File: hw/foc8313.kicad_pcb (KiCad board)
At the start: 2 copper layers, 70 parts, among them CN1 XT30PW-M, CN2 XT30PW-M, J1 Tag Connect, J2 CAN, J3 CAN, P1 USB_C_Plug, U1 DRV8313PWP, U10 XC6206P332MR, U2 STM32F103CBTx, U3 AS5047D, U4 INA240A2D, U5 INA240A2D, U7 LMR36015SFBRNXR, U8 INA240A2D, U9 ADM3053BRW_C579192, X1 X322516MLB4SI

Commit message: WIP XT30?
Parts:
- added FB1: 1.8k@100MHz, Resistor_SMD:R_0402_1005Metric, F.Cu at (190.2, 110.7)
- added FB2: 1.8k@100MHz, Resistor_SMD:R_0402_1005Metric, F.Cu at (190.2, 112.7)
- added U6: MR30PW-M30.G.Y, easyeda:CONN-TH_MR30PW-M30-G-Y, F.Cu at (140.6, 112.0)
- C20, C4, C7, P1, R12, R15, R4, R8, U3: moved to B.Cu
- J2, J3: footprint Connector_JST:JST_GH_SM04B-GHS-TB_1x04-1MP_P1.25mm_Horizontal -> Connector_JST:JST_GH_SM03B-GHS-TB_1x03-1MP_P1.25mm_Horizontal; moved to B.Cu
- moved U9 86.9 mm to (127.3, 101.7), turned to -90 degrees
- moved CN1 86.3 mm to (127.0, 86.5), turned to 180 degrees
- moved CN2 74.7 mm to (153.2, 86.5), turned to 180 degrees
- moved D2 68.5 mm to (118.0, 19.0)
- moved C10 68.5 mm to (98.5, 16.3)
- moved C12 68.5 mm to (98.5, 21.4)
- moved C13 68.5 mm to (98.5, 23.9)
- moved C14 68.5 mm to (117.3, 21.2)
- moved C15 68.5 mm to (117.3, 23.2)
- moved C22 68.5 mm to (115.5, 30.9)
- moved C23 68.5 mm to (94.5, 51.3)
- moved C26 68.5 mm to (115.4, 51.3)
- moved C3 68.5 mm to (94.5, 21.4)
- moved C5 68.5 mm to (94.5, 23.9)
- moved C8 68.5 mm to (94.5, 31.4)
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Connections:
- C1 pad 2: +3.3V -> GND
- C10 pad 2: +3.3V -> GND
- C11 pad 2: +3.3V -> GND
- C12 pad 2: +3.3V -> GND
- C13 pad 2: +3.3V -> GND
- C14 pad 2: +3.3V -> GND
- C15 pad 1: +3.3V -> GND
- C16 pad 2: +3.3V -> GND
- C17 pad 2: +3.3V -> GND
- C19 pad 2: +3.3V -> GND
- C2 pad 2: +3.3V -> GND
- C20 pad 2: +3.3V -> GND
- C22 pad 2: +3.3V -> GND
- C23 pad 2: +3.3V -> GND
- C24 pad 2: +3.3V -> GND
- C26 pad 2: +3.3V -> GND
- C27 pad 2: +3.3V -> GND
- C30 pad 2: +3.3V -> GND
- C31 pad 2: +3.3V -> GND
- C32 pad 2: +3.3V -> GND
- C33 pad 2: +3.3V -> GND
- C4 pad 2: +3.3V -> GND
- C5 pad 2: +3.3V -> GND
- C6 pad 2: +3.3V -> GND
- C7 pad 2: +3.3V -> GND
- C9 pad 2: +3.3V -> GND
- CN1 pad 1: +3.3V -> VCC
- CN1 pad 2: VCC -> GND
- CN2 pad 1: +3.3V -> VCC
- CN2 pad 2: VCC -> GND
- J1 pad 5: +3.3V -> GND
- P1 pad A1: +3.3V -> GND
- P1 pad A12: +3.3V -> GND
- P1 pad B1: +3.3V -> GND
- P1 pad B12: +3.3V -> GND
- R11 pad 2: +3.3V -> GND
- R13 pad 2: +3.3V -> GND
- R3 pad 1: +3.3V -> GND
- R5 pad 2: +3.3V -> GND
- U1 pad 10: +3.3V -> GND
- U1 pad 14: +3.3V -> GND
- U1 pad 20: +3.3V -> GND
- U1 pad 28: +3.3V -> GND
- U1 pad 29: +3.3V -> GND
- U1 pad 6: +3.3V -> GND
- U1 pad 7: +3.3V -> GND
- U10 pad 1: +3.3V -> GND
- U2 pad 23: +3.3V -> GND
- U2 pad 35: +3.3V -> GND
- U2 pad 47: +3.3V -> GND
- U3 pad 13: +3.3V -> GND
- U3 pad 5: +3.3V -> GND
- U4 pad 2: +3.3V -> GND
- U4 pad 3: +3.3V -> GND
- U4 pad 4: +3.3V -> GND
- U5 pad 2: +3.3V -> GND
- U5 pad 3: +3.3V -> GND
- U5 pad 4: +3.3V -> GND
- U7 pad 1: +3.3V -> GND
- U7 pad 11: +3.3V -> GND
- U7 pad 6: +3.3V -> GND
- U8 pad 2: +3.3V -> GND
- U8 pad 3: +3.3V -> GND
- U8 pad 4: +3.3V -> GND
- U9 pad 1: +3.3V -> GND
- U9 pad 10: +3.3V -> GND
- U9 pad 3: +3.3V -> GND
- U9 pad 7: +3.3V -> GND
- U9 pad 9: +3.3V -> GND
- X1 pad 2: +3.3V -> GND
- X1 pad 4: +3.3V -> GND
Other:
- board outline added: 40 x 40 mm

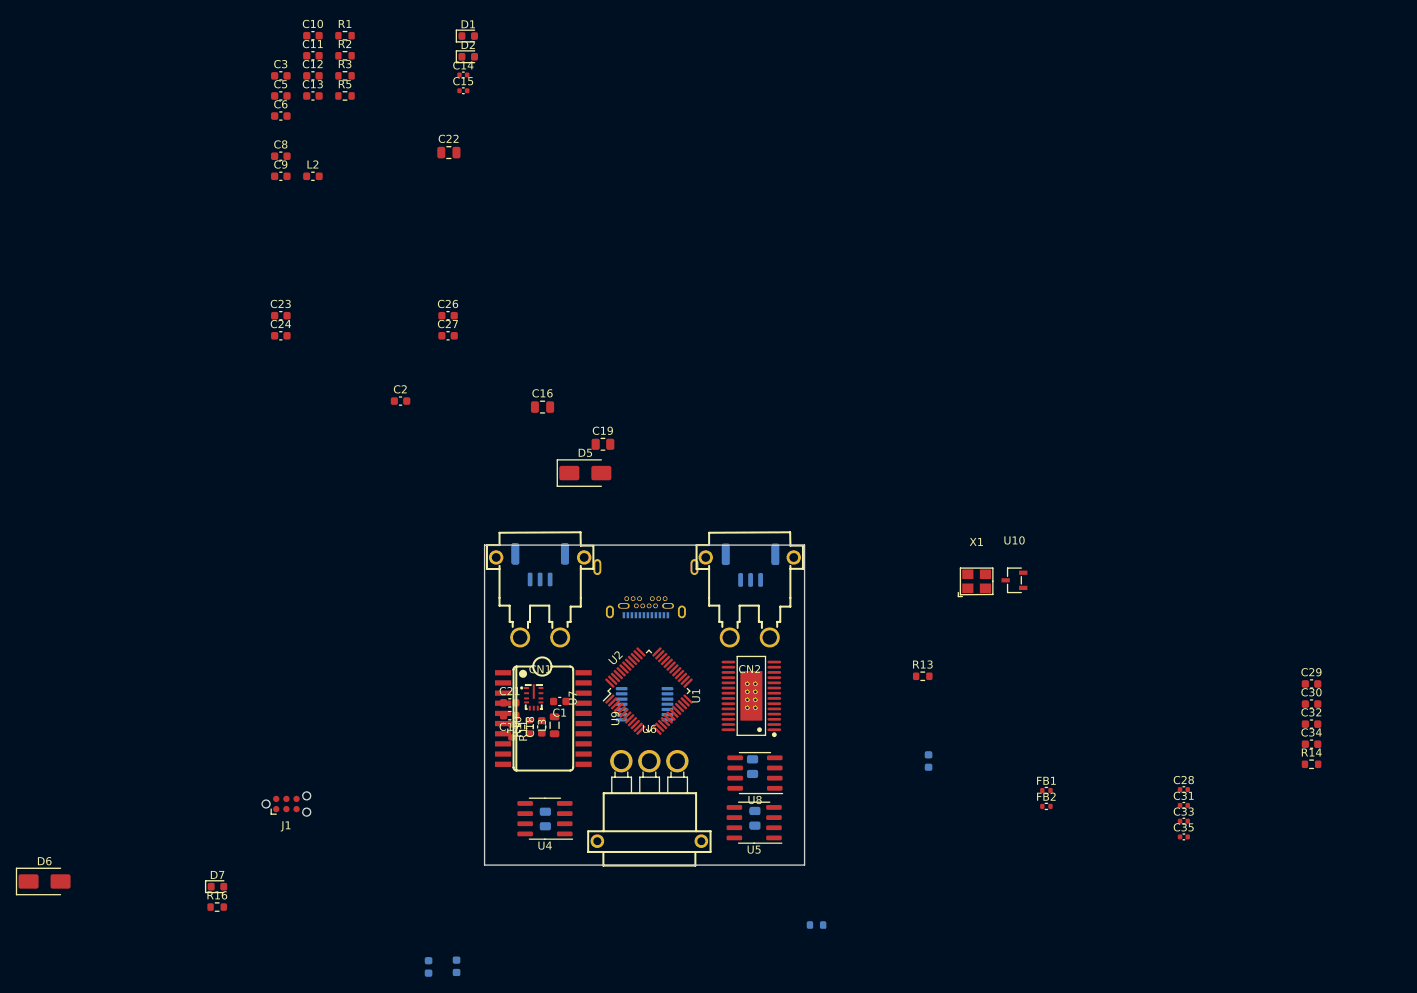
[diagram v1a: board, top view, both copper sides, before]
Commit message: [Hw] No iso can, 0402 where possible, approx layout and formfactor
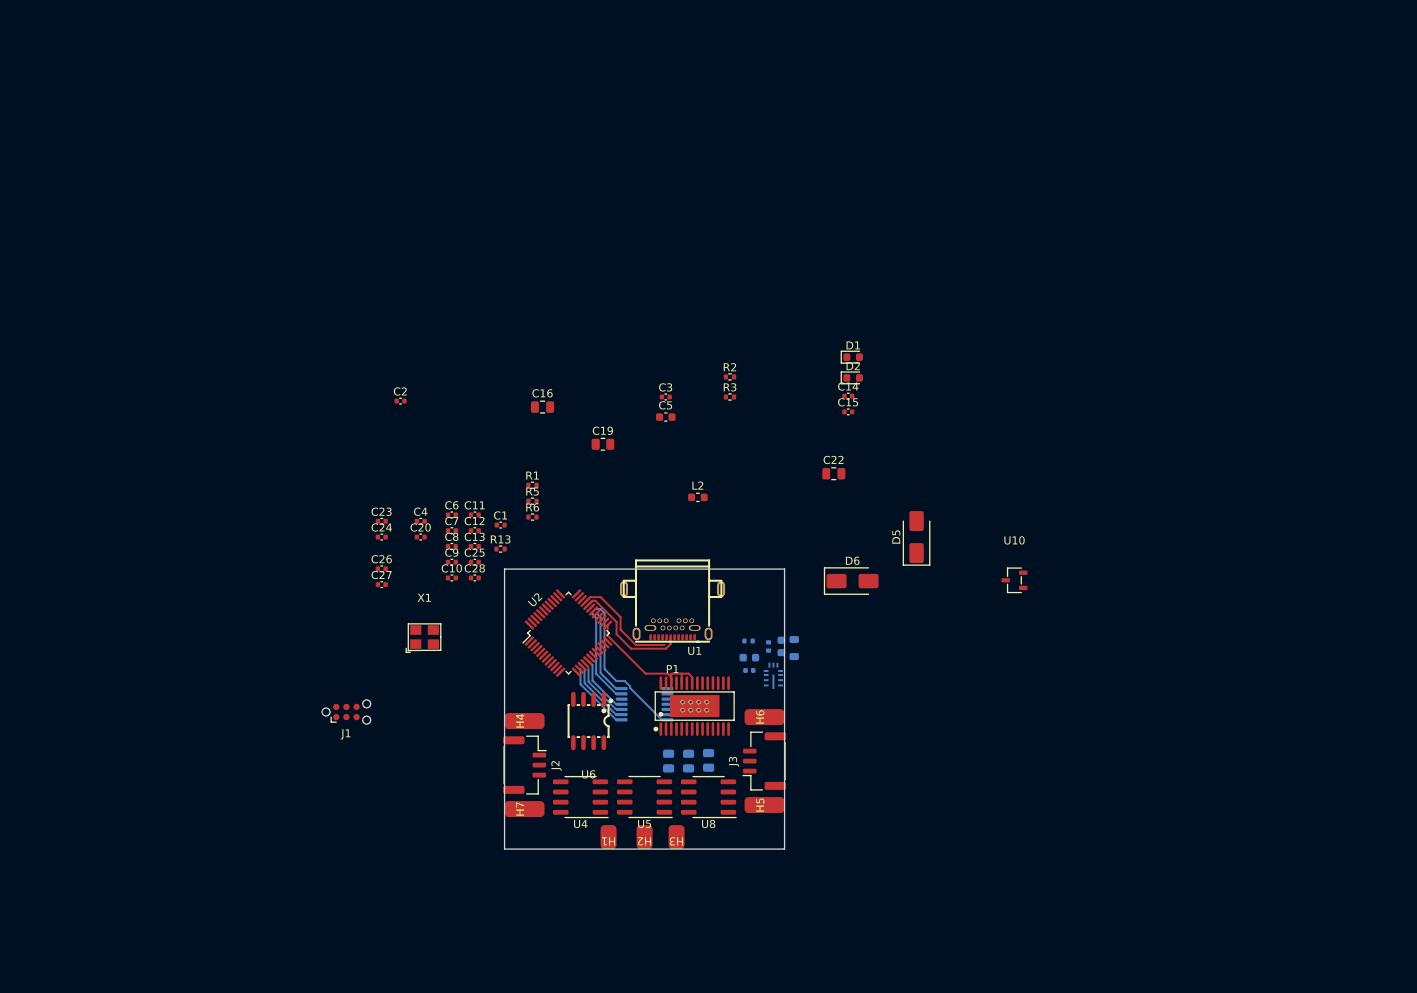
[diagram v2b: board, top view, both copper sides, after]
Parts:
- removed C29, C30, C32, C34: 10u, Capacitor_SMD:C_0603_1608Metric
- removed C31, C33, C35: 100n, Capacitor_SMD:C_0402_1005Metric
- removed CN1, CN2: XT30PW-M, easyeda:CONN-TH_XT30PW-M
- removed D7: BLUE, LED_SMD:LED_0603_1608Metric
- removed FB1, FB2: 1.8k@100MHz, Resistor_SMD:R_0402_1005Metric
- removed R12: 100k, Resistor_SMD:R_0603_1608Metric
- removed R14: 120, Resistor_SMD:R_0603_1608Metric
- removed R16: 1k5, Resistor_SMD:R_0603_1608Metric
- removed U9: ADM3053BRW_C579192, easyeda:SO-20_L12.8-W7.5-P1.27-LS10.3-BL
- added C25: 100n, Capacitor_SMD:C_0402_1005Metric, F.Cu at (118.8, 82.1)
- added H1: MountingHole_Pad, local_lib:2x3, F.Cu at (135.5, 116.5)
- added H2: MountingHole_Pad, local_lib:2x3, F.Cu at (140.0, 116.5)
- added H3: MountingHole_Pad, local_lib:2x3, F.Cu at (144.0, 116.5)
- added H4: MountingHole_Pad, local_lib:2x5, F.Cu at (125.0, 102.0)
- added H5: MountingHole_Pad, local_lib:2x5, F.Cu at (155.0, 112.5)
- added H6: MountingHole_Pad, local_lib:2x5, F.Cu at (155.0, 101.5)
- added H7: MountingHole_Pad, local_lib:2x5, F.Cu at (125.0, 113.0)
- added R6: 100k, Resistor_SMD:R_0402_1005Metric, F.Cu at (126.0, 76.5)
- C1, C10, C11, C12, C13, C2, C23, C24, C26, C27, C3, C6, C8, C9: footprint Capacitor_SMD:C_0603_1608Metric -> Capacitor_SMD:C_0402_1005Metric
- C17, C18, L3, U7: moved to B.Cu
- C20, C4, C7: footprint Capacitor_SMD:C_0603_1608Metric -> Capacitor_SMD:C_0402_1005Metric; moved to F.Cu
- C21: footprint Capacitor_SMD:C_0603_1608Metric -> Capacitor_SMD:C_0402_1005Metric; moved to B.Cu
- J2, J3, P1: moved to F.Cu
- R1, R13, R2, R3, R5: footprint Resistor_SMD:R_0603_1608Metric -> Resistor_SMD:R_0402_1005Metric
- R10, R11: footprint Resistor_SMD:R_0603_1608Metric -> Resistor_SMD:R_0402_1005Metric; moved to B.Cu
- U6: value MR30PW-M30.G.Y -> TJA1044GT/3Z; footprint easyeda:CONN-TH_MR30PW-M30-G-Y -> easyeda:SO-8_L4.9-W3.9-P1.27-LS5.9-BL
- moved D6 107.8 mm to (166.0, 84.5)
- moved C28 92.5 mm to (118.8, 84.1)
- moved C10 70.0 mm to (115.9, 84.1)
- moved X1 69.4 mm to (112.5, 91.5)
- moved C7 66.2 mm to (115.9, 78.2), turned to 0 degrees
- moved C14 62.7 mm to (165.5, 61.4)
- moved C15 62.7 mm to (165.5, 63.4)
- moved C22 62.7 mm to (163.7, 71.1)
- moved C3 62.7 mm to (142.7, 61.5)
- moved C5 62.7 mm to (142.7, 64.0)
- moved R2 62.7 mm to (150.7, 59.0)
- moved R3 62.7 mm to (150.7, 61.5)
- moved D1 62.7 mm to (166.1, 56.5)
- moved D2 62.7 mm to (166.1, 59.1)
- moved L2 62.7 mm to (146.7, 74.0)
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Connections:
- C28 pad 1: /isocan/ISOGND -> +3.3V
- C28 pad 2: /isocan/CAN.V+ -> GND
- U6 pad 1: /OUTA -> /CAN.TX
- U6 pad 2: /OUTB -> GND
- U6 pad 3: /OUTC -> +5V
- U6 pad 4: unconnected-(U6-Pad4) -> /CAN.RX
- U6 pad 5: unconnected-(U6-Pad5) -> +3.3V
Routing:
- net /ENC_Z: track 0.00 -> 18.8 mm
- net /DRV_EN: track 0.00 -> 18.0 mm
- net /USB_DM: track 0.00 -> 15.0 mm
- net /USB_DP: track 0.00 -> 13.6 mm
- net /ENC_B: track 0.00 -> 12.0 mm
- net /ENC_A: track 0.00 -> 11.2 mm
- net /~{SPI1_NSS}: track 0.00 -> 8.88 mm
- net /SPI1_SCLK: track 0.00 -> 8.02 mm
- net /SPI1_MOSI: track 0.00 -> 7.52 mm
- net /SPI1_MISO: track 0.00 -> 7.17 mm
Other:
- board size 40 x 40 mm -> 35 x 35 mm

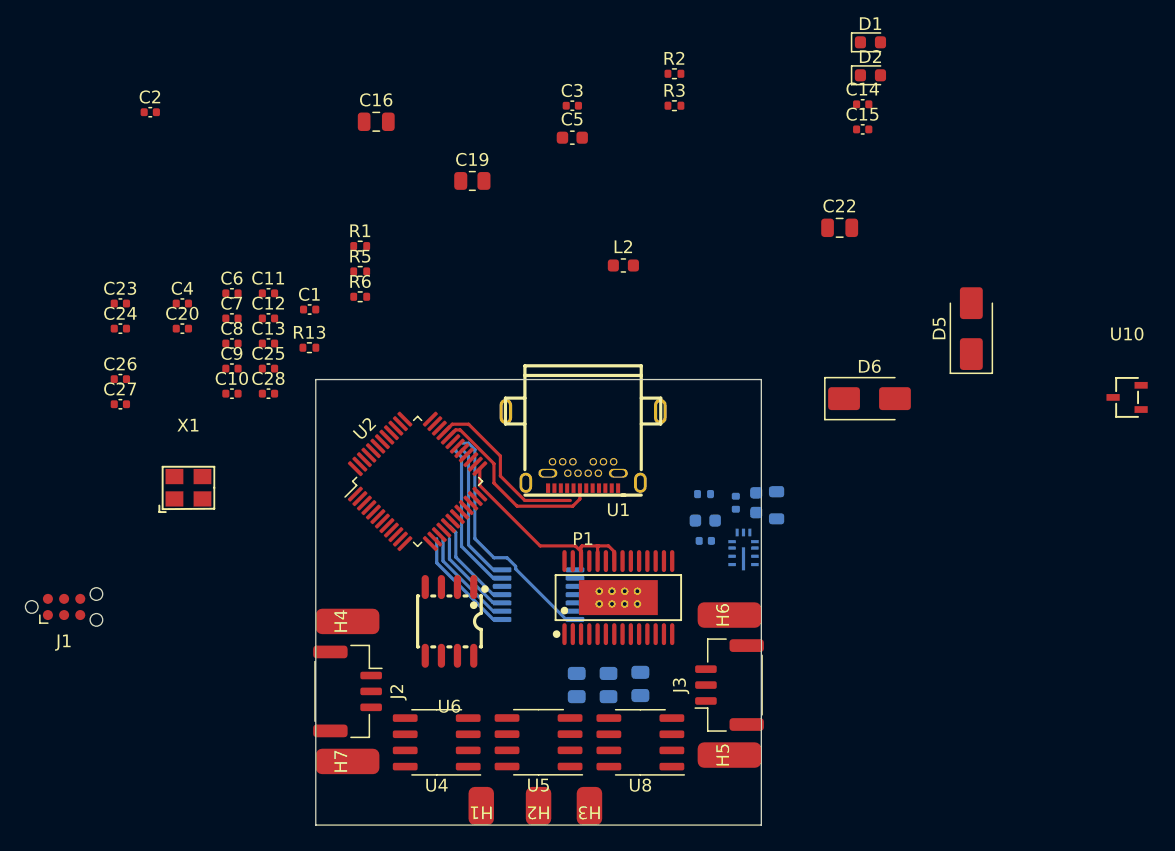
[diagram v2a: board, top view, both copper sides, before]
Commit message: [Hw] Rough incomplete layout and component placement
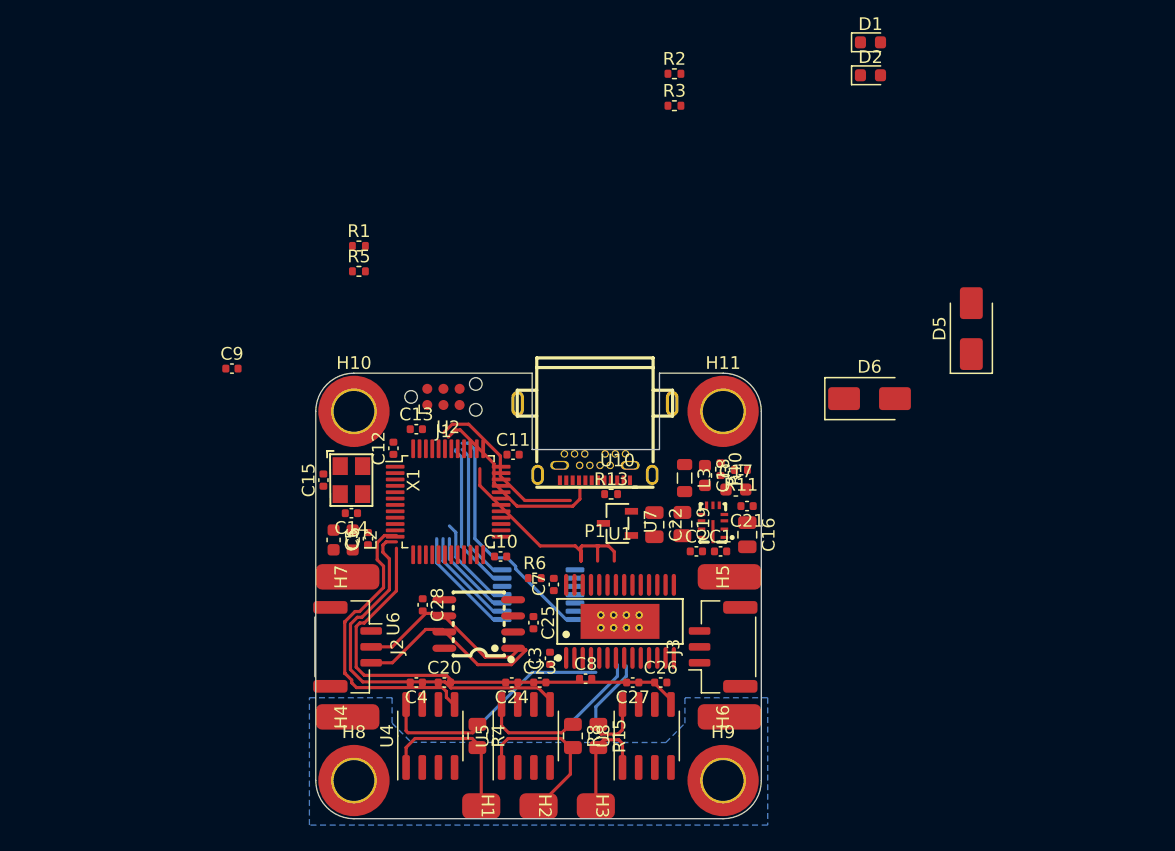
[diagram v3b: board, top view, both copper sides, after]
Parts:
- added H10: MountingHole, MountingHole:MountingHole_3.2mm_M3_DIN965_Pad_TopOnly, F.Cu at (125.5, 85.5)
- added H11: MountingHole, MountingHole:MountingHole_3.2mm_M3_DIN965_Pad_TopOnly, F.Cu at (154.5, 85.5)
- added H8: MountingHole, MountingHole:MountingHole_3.2mm_M3_DIN965_Pad_TopOnly, F.Cu at (125.5, 114.5)
- added H9: MountingHole, MountingHole:MountingHole_3.2mm_M3_DIN965_Pad_TopOnly, F.Cu at (154.5, 114.5)
- C17, C18, C21, L3, R10, R11, R15, R4, R8, U7: moved to F.Cu
- moved C2 55.1 mm to (152.4, 96.5)
- moved C14 51.4 mm to (125.3, 93.5), turned to 180 degrees
- moved C15 50.5 mm to (123.1, 90.9), turned to 90 degrees
- moved C26 48.7 mm to (149.6, 106.8)
- moved C27 45.8 mm to (147.4, 106.8), turned to 180 degrees
- moved C23 44.4 mm to (140.1, 106.8)
- moved C16 43.6 mm to (156.4, 95.2), turned to -90 degrees
- moved C3 43.4 mm to (140.9, 104.9), turned to 90 degrees
- moved C24 41.5 mm to (137.9, 106.8), turned to 180 degrees
- moved U10 41.2 mm to (146.2, 94.3)
- moved C8 38.3 mm to (143.7, 106.5)
- moved C1 37.5 mm to (154.3, 96.5)
- moved C5 36.7 mm to (123.9, 95.6), turned to -90 degrees
- moved C4 35.0 mm to (130.4, 106.8), turned to 180 degrees
- moved C20 34.6 mm to (132.6, 106.8)
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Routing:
- net /ISENSE_C: track 0.00 -> 37.0 mm
- net /ISENSE_B: track 0.00 -> 29.7 mm
- net /ISENSE_A: track 0.00 -> 23.8 mm
- net (no net): track 0.00 -> 16.8 mm
- net /CAN.H: track 0.00 -> 14.9 mm
- net /CAN.L: track 0.00 -> 14.2 mm
- net /OUTB: track 0.00 -> 13.3 mm
- net /OUTA: track 0.00 -> 12.6 mm
- net /PHC: track 0.00 -> 10.7 mm
- net /OUTC: track 0.00 -> 8.94 mm
- net /PHA: track 0.00 -> 8.31 mm
- net /PHB: track 0.00 -> 7.67 mm
- added copper zone on In1.Cu, net GND
- added copper zone on In2.Cu, net GND
- added copper zone on In1.Cu, net GNDA
- added copper zone on B.Cu, net VCC
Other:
- outline, holes or cut-outs redrawn
- copper layers 2 -> 4
